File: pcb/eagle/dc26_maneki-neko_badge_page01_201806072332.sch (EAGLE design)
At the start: 55 parts, among them T1 RK7002BMT116, U1 STM32F030C8T, U2 PAM2301CAAB330, U3 NPTC042KFMS-RC, U5 MIC2005A-1YM5-TR, U6 MIC2005A-1YM5-TR

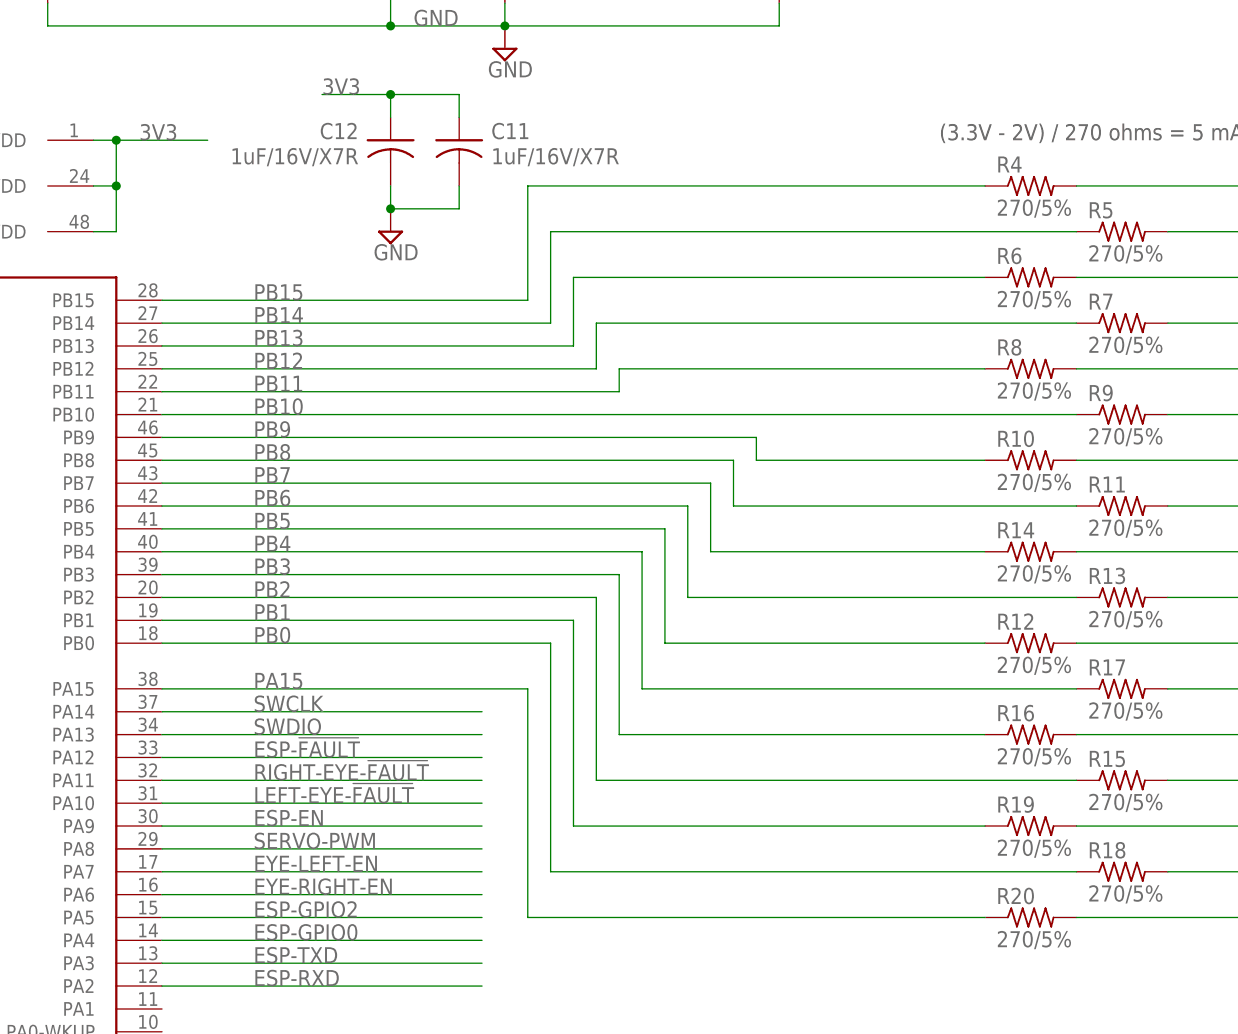
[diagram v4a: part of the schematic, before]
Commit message: re-orging traces to eyes for clean routing, done routing left eye
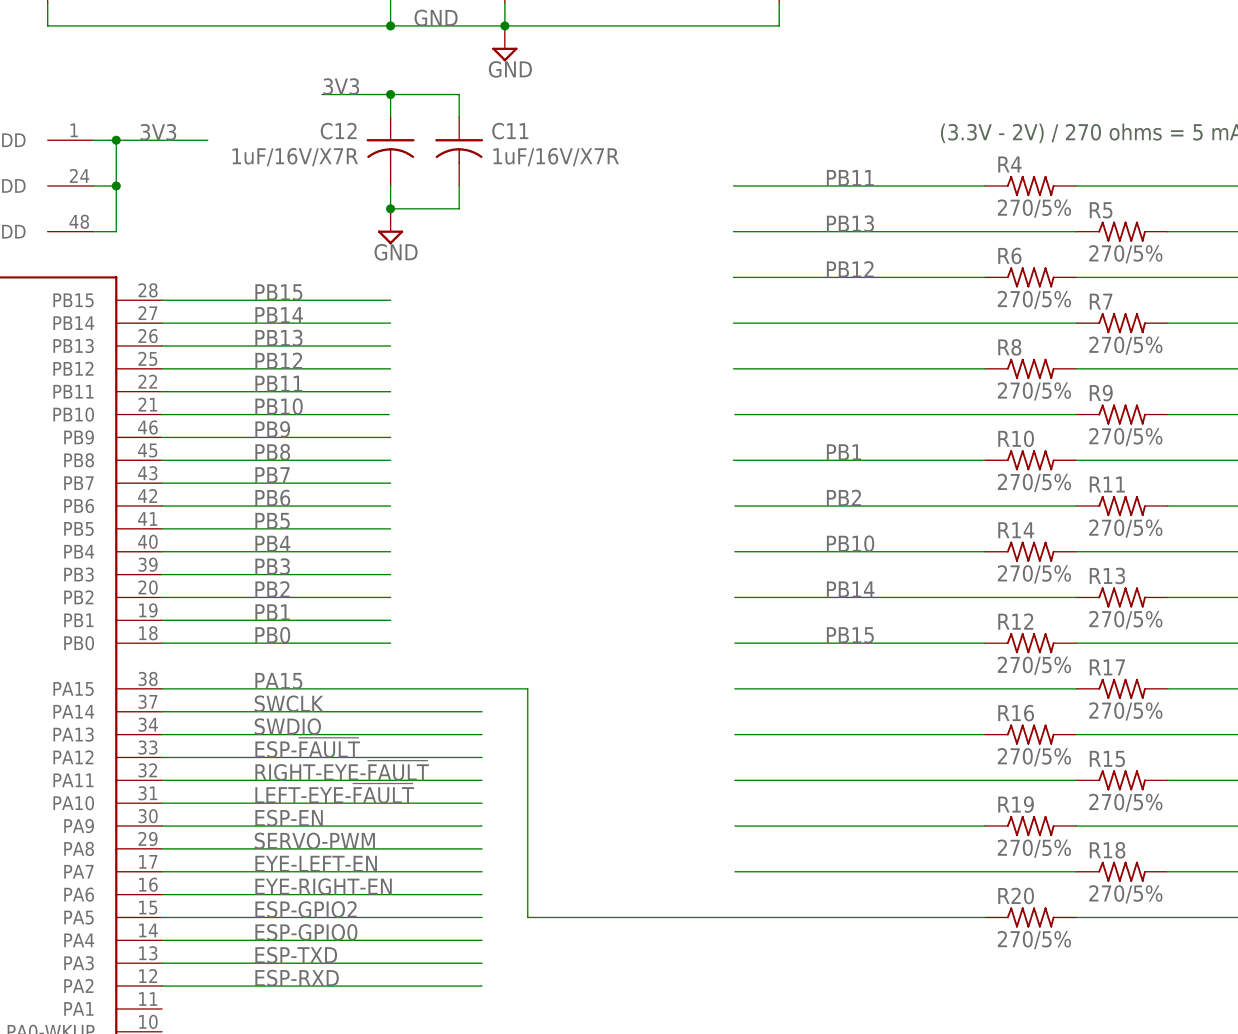
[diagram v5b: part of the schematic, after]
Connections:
- new net N$: R7.1
- new net N$14: R17.1
- new net N$15: R16.1
- new net N$19: R9.1
- new net N$8: R8.1
- net PB1: now also R10.1
- net PB10: now also R14.1; no longer R9.1
- net PB11: now also R4.1; no longer R8.1
- net PB12: now also R6.1; no longer R7.1
- net PB13: now also R5.1; no longer R6.1
- net PB14: now also R13.1; no longer R5.1
- net PB15: now also R12.1; no longer R4.1
- net PB2: now also R11.1
- net PB3: no longer R16.1
- net PB4: no longer R17.1
- net PB5: no longer R12.1
- net PB6: no longer R13.1
- net PB7: no longer R14.1
- net PB8: no longer R11.1
- net PB9: no longer R10.1

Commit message: all led and high(er) speed signals routed... phewf
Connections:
- removed net N$: R7.1
- removed net N$14: R17.1
- removed net N$15: R16.1
- removed net N$19: R9.1
- removed net N$8: R8.1
- net PB1: no longer R19.1
- net PB2: no longer R15.1
- net PB3: now also R17.1
- net PB4: now also R16.1
- net PB5: now also R7.1
- net PB6: now also R8.1
- net PB7: now also R15.1
- net PB8: now also R9.1
- net PB9: now also R19.1
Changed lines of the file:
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@@
 <label x="-111.76" y="162.56" size="1.778" layer="95"/>
+</segment>
+<segment>
+<pinref part="R19" gate="G$1" pin="1"/>
+<wire x1="-30.48" y1="119.38" x2="-58.42" y2="119.38" width="0.1524" layer="91"/>
+<label x="-48.26" y="119.38" size="1.778" layer="95"/>
 </segment>
 </net>
@@
 <label x="-111.76" y="160.02" size="1.778" layer="95"/>
 </segment>
+<segment>
+<pinref part="R9" gate="G$1" pin="1"/>
+<wire x1="-20.32" y1="165.1" x2="-58.42" y2="165.1" width="0.1524" layer="91"/>
+<label x="-48.26" y="165.1" size="1.778" layer="95"/>
+</segment>
 </net>
 <net name="PB7" class="0">
@@
 <label x="-111.76" y="157.48" size="1.778" layer="95"/>
 </segment>
+<segment>
+<pinref part="R15" gate="G$1" pin="1"/>
+<wire x1="-20.32" y1="124.46" x2="-58.42" y2="124.46" width="0.1524" layer="91"/>
+<label x="-48.26" y="124.46" size="1.778" layer="95"/>
+</segment>
 </net>
 <net name="PB6" class="0">
@@
 <label x="-111.76" y="154.94" size="1.778" layer="95"/>
 </segment>
+<segment>
+<pinref part="R8" gate="G$1" pin="1"/>
+<wire x1="-30.48" y1="170.18" x2="-58.42" y2="170.18" width="0.1524" layer="91"/>
+<label x="-48.26" y="170.18" size="1.778" layer="95"/>
+</segment>
 </net>
 <net name="PB5" class="0">
@@
 <label x="-111.76" y="152.4" size="1.778" layer="95"/>
 </segment>
+<segment>
+<pinref part="R7" gate="G$1" pin="1"/>
+<wire x1="-20.32" y1="175.26" x2="-58.42" y2="175.26" width="0.1524" layer="91"/>
+<label x="-48.26" y="175.26" size="1.778" layer="95"/>
+</segment>
 </net>
 <net name="PB4" class="0">
@@
 <label x="-111.76" y="149.86" size="1.778" layer="95"/>
 </segment>
+<segment>
+<pinref part="R16" gate="G$1" pin="1"/>
+<wire x1="-30.48" y1="129.54" x2="-58.42" y2="129.54" width="0.1524" layer="91"/>
+<label x="-48.26" y="129.54" size="1.778" layer="95"/>
+</segment>
 </net>
 <net name="PB3" class="0">
@@
 <label x="-111.76" y="147.32" size="1.778" layer="95"/>
 </segment>
+<segment>
+<pinref part="R17" gate="G$1" pin="1"/>
+<wire x1="-20.32" y1="134.62" x2="-58.42" y2="134.62" width="0.1524" layer="91"/>
+<label x="-48.26" y="134.62" size="1.778" layer="95"/>
+</segment>
 </net>
 <net name="PB2" class="0">
-<segment>
-<pinref part="R15" gate="G$1" pin="1"/>
-<wire x1="-58.2676" y1="124.46" x2="-20.32" y2="124.46" width="0.1524" layer="91"/>
-</segment>
 <segment>
 <pinref part="U1" gate="MCU" pin="PB2"/>
@@
 <net name="PB1" class="0">
 <segment>
-<pinref part="R19" gate="G$1" pin="1"/>
-<wire x1="-30.48" y1="119.38" x2="-58.2676" y2="119.38" width="0.1524" layer="91"/>
-</segment>
-<segment>
 <pinref part="U1" gate="MCU" pin="PB1"/>
 <wire x1="-96.52" y1="142.24" x2="-121.92" y2="142.24" width="0.1524" layer="91"/>
@@
 <net name="PB0" class="0">
 <segment>
-<pinref part="R18" gate="G$1" pin="1"/>
-<wire x1="-58.2676" y1="114.3" x2="-20.32" y2="114.3" width="0.1524" layer="91"/>
-</segment>
-<segment>
 <pinref part="U1" gate="MCU" pin="PB0"/>
 <wire x1="-121.92" y1="139.7" x2="-96.52" y2="139.7" width="0.1524" layer="91"/>
 <label x="-111.76" y="139.7" size="1.778" layer="95"/>
+</segment>
+<segment>
+<pinref part="R18" gate="G$1" pin="1"/>
+<wire x1="-20.32" y1="114.3" x2="-58.42" y2="114.3" width="0.1524" layer="91"/>
+<label x="-48.26" y="114.3" size="1.778" layer="95"/>
 </segment>
 </net>
@@
 </segment>
 </net>
-<net name="N$8" class="0">
-<segment>
-<pinref part="R8" gate="G$1" pin="1"/>
-<wire x1="-30.48" y1="170.18" x2="-58.42" y2="170.18" width="0.1524" layer="91"/>
-</segment>
-</net>
-<net name="N$14" class="0">
-<segment>
-<pinref part="R17" gate="G$1" pin="1"/>
-<wire x1="-58.2676" y1="134.62" x2="-20.32" y2="134.62" width="0.1524" layer="91"/>
-</segment>
-</net>
-<net name="N$15" class="0">
-<segment>
-<pinref part="R16" gate="G$1" pin="1"/>
-<wire x1="-30.48" y1="129.54" x2="-58.2676" y2="129.54" width="0.1524" layer="91"/>
-</segment>
-</net>
-<net name="N$19" class="0">
-<segment>
-<pinref part="R9" gate="G$1" pin="1"/>
-<wire x1="-58.2676" y1="165.1" x2="-20.32" y2="165.1" width="0.1524" layer="91"/>
-</segment>
-</net>
-<net name="N$" class="0">
-<segment>
-<pinref part="R7" gate="G$1" pin="1"/>
-<wire x1="-58.42" y1="175.26" x2="-20.32" y2="175.26" width="0.1524" layer="91"/>
-</segment>
-</net>

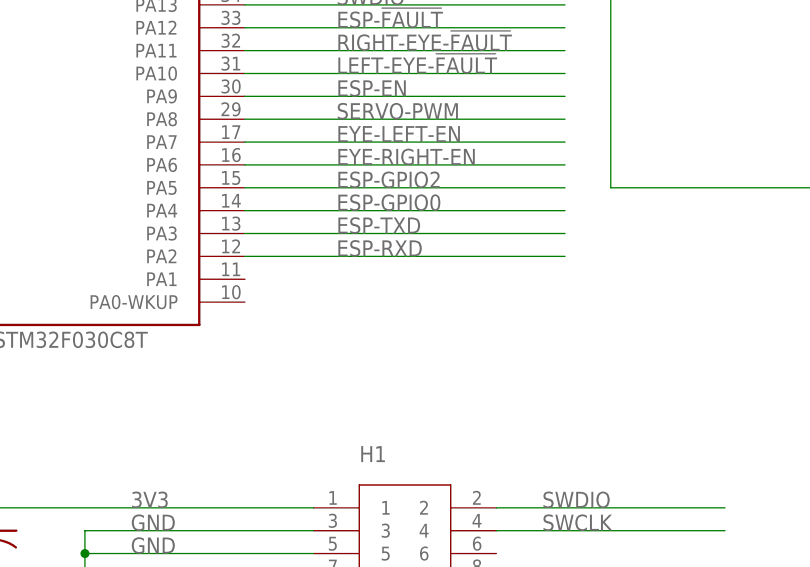
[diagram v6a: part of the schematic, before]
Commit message: pcb traces routed, just need to finish off GND and 3V3 rails
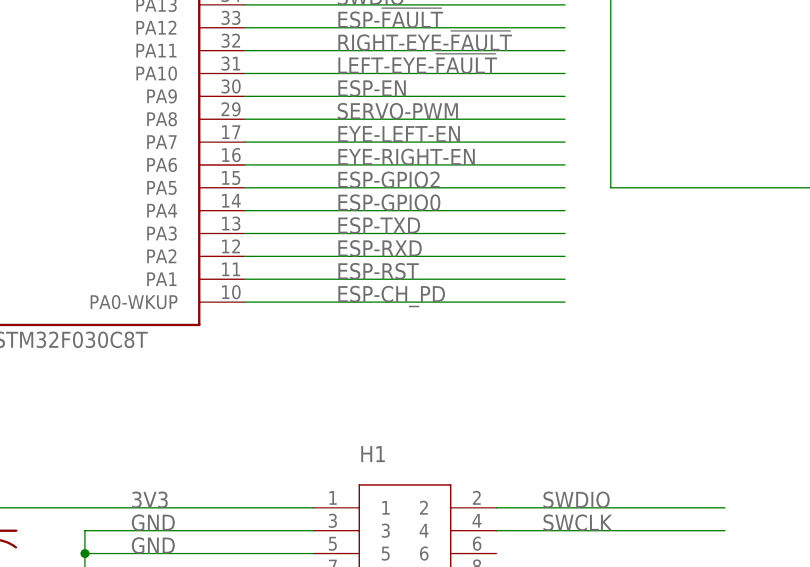
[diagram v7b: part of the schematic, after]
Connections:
- net ESP-CH_PD: now also U1MCU.PA0-WKUP
- net ESP-RST: now also U1MCU.PA1
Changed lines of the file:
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@@
 <pinref part="U3" gate="G$1" pin="CH_PD"/>
+</segment>
+<segment>
+<pinref part="U1" gate="MCU" pin="PA0-WKUP"/>
+<wire x1="-121.92" y1="96.52" x2="-86.36" y2="96.52" width="0.1524" layer="91"/>
+<label x="-111.76" y="96.52" size="1.778" layer="95"/>
 </segment>
 </net>
@@
 <pinref part="U3" gate="G$1" pin="RST"/>
 </segment>
+<segment>
+<pinref part="U1" gate="MCU" pin="PA1"/>
+<wire x1="-121.92" y1="99.06" x2="-86.36" y2="99.06" width="0.1524" layer="91"/>
+<label x="-111.76" y="99.06" size="1.778" layer="95"/>
+</segment>
 </net>

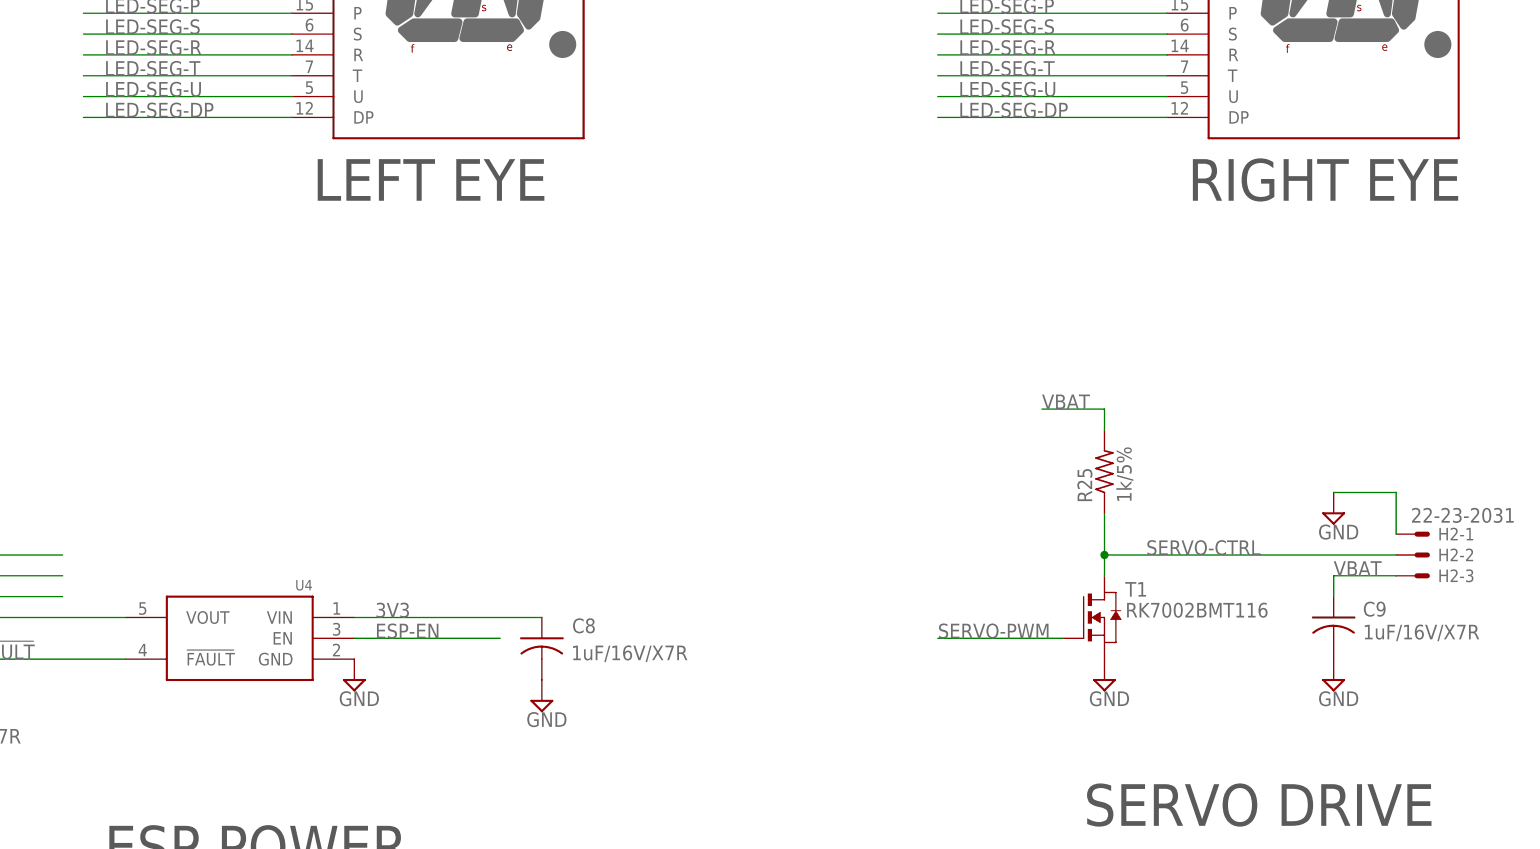
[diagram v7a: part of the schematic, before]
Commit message: silk fixed, drc errors fixed, going to export and send thru freedfm
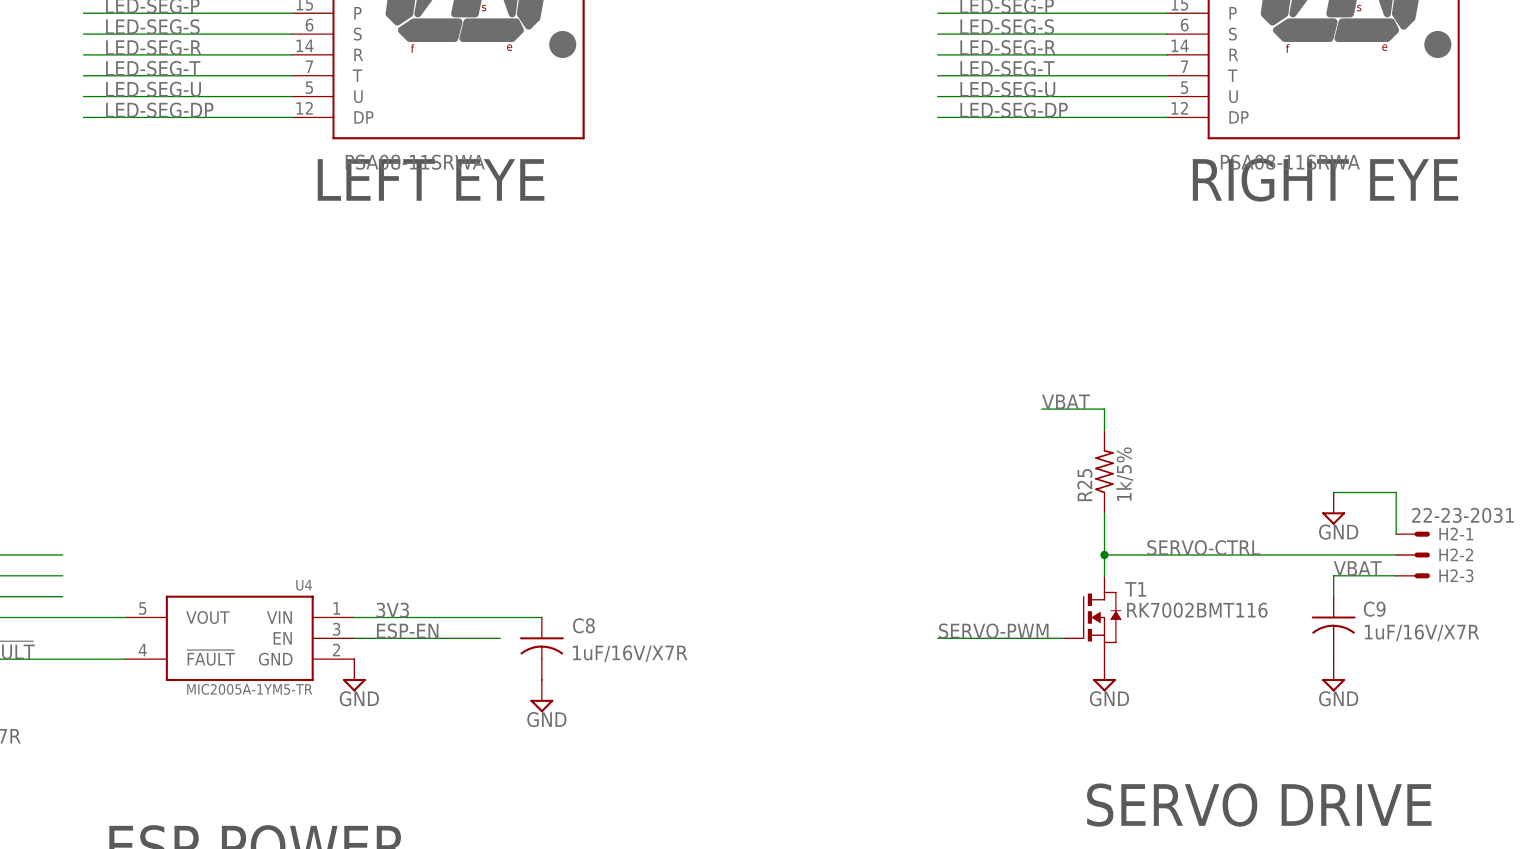
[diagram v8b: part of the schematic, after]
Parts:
- D1, D2: value (none) -> PSA08-11SRWA
- U4: value (none) -> MIC2005A-1YM5-TR
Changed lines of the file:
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@@
 <part name="R19" library="rcl" library_urn="urn:adsk.eagle:library:334" deviceset="R-US_" device="R0805" package3d_urn="urn:adsk.eagle:package:23553/2" value="270/5%"/>
 <part name="R18" library="rcl" library_urn="urn:adsk.eagle:library:334" deviceset="R-US_" device="R0805" package3d_urn="urn:adsk.eagle:package:23553/2" value="270/5%"/>
-<part name="D1" library="PSA08-11SRWA" deviceset="PSA08-11SRWA" device=""/>
-<part name="D2" library="PSA08-11SRWA" deviceset="PSA08-11SRWA" device=""/>
+<part name="D1" library="PSA08-11SRWA" deviceset="PSA08-11SRWA" device="" value="PSA08-11SRWA"/>
+<part name="D2" library="PSA08-11SRWA" deviceset="PSA08-11SRWA" device="" value="PSA08-11SRWA"/>
 <part name="U6" library="MIC2005A-1YM5-TR" deviceset="MIC2005A-1YM5-TR" device="" value="MIC2005A-1YM5-TR"/>
 <part name="U5" library="MIC2005A-1YM5-TR" deviceset="MIC2005A-1YM5-TR" device="" value="MIC2005A-1YM5-TR"/>
@@
 <part name="SUPPLY8" library="supply2" library_urn="urn:adsk.eagle:library:372" deviceset="GND" device=""/>
 <part name="SUPPLY9" library="supply2" library_urn="urn:adsk.eagle:library:372" deviceset="GND" device=""/>
-<part name="U4" library="MIC2005A-1YM5-TR" deviceset="MIC2005A-1YM5-TR" device=""/>
+<part name="U4" library="MIC2005A-1YM5-TR" deviceset="MIC2005A-1YM5-TR" device="" value="MIC2005A-1YM5-TR"/>
 <part name="SUPPLY10" library="supply2" library_urn="urn:adsk.eagle:library:372" deviceset="GND" device=""/>
 <part name="C8" library="rcl" library_urn="urn:adsk.eagle:library:334" deviceset="C-US" device="C0805" package3d_urn="urn:adsk.eagle:package:23617/2" value="1uF/16V/X7R"/>
@@
 </sheet>
 </sheets>
+<errors>
+</errors>
 </schematic>
 </drawing>
